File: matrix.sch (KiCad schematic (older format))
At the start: 173 parts

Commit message: Add indicator LEDs
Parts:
- KBP1-1: footprint MX_Only:MXOnly-2U -> MX_Only:MXOnly-1U
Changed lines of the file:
@@
 F 0 "KBP1-1" H 12900 936 50  0000 C CNN
 F 1 "Keyboard_Switch" H 12900 1000 50  0001 C CNN
-F 2 "MX_Only:MXOnly-2U" H 12900 1105 50  0001 C CNN
+F 2 "MX_Only:MXOnly-1U" H 12900 1105 50  0001 C CNN
 F 3 "" H 12900 1105 50  0001 C CNN
 	2    12900 1100

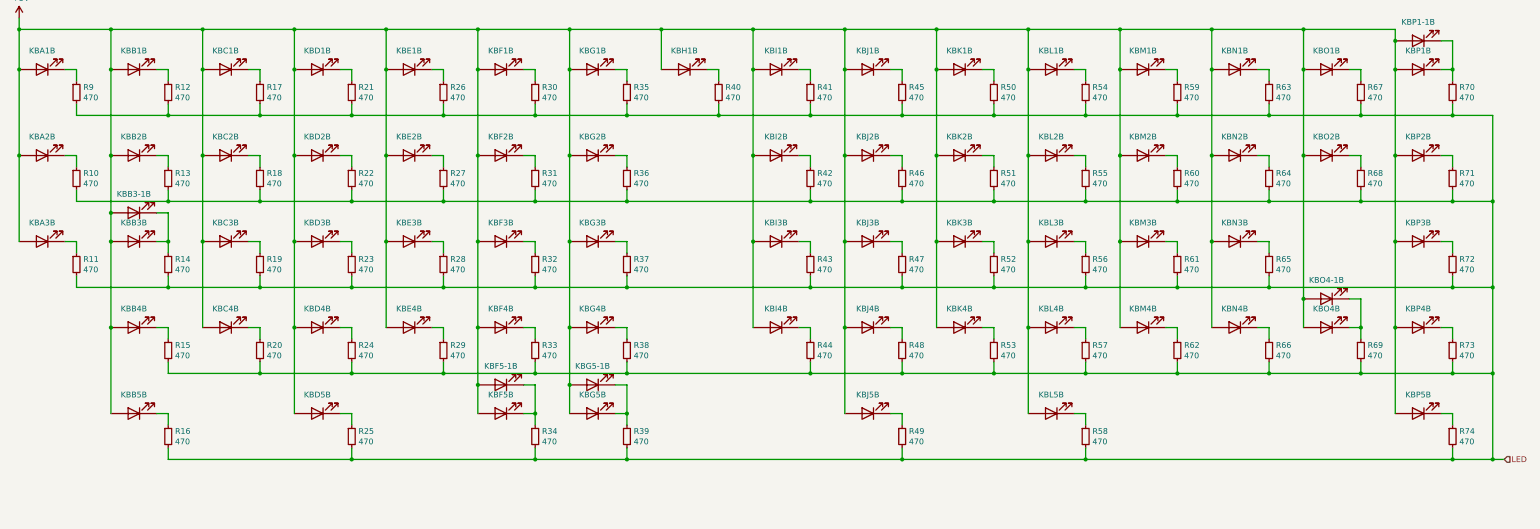
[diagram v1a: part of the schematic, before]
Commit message: Lay out switch and LED matrix components
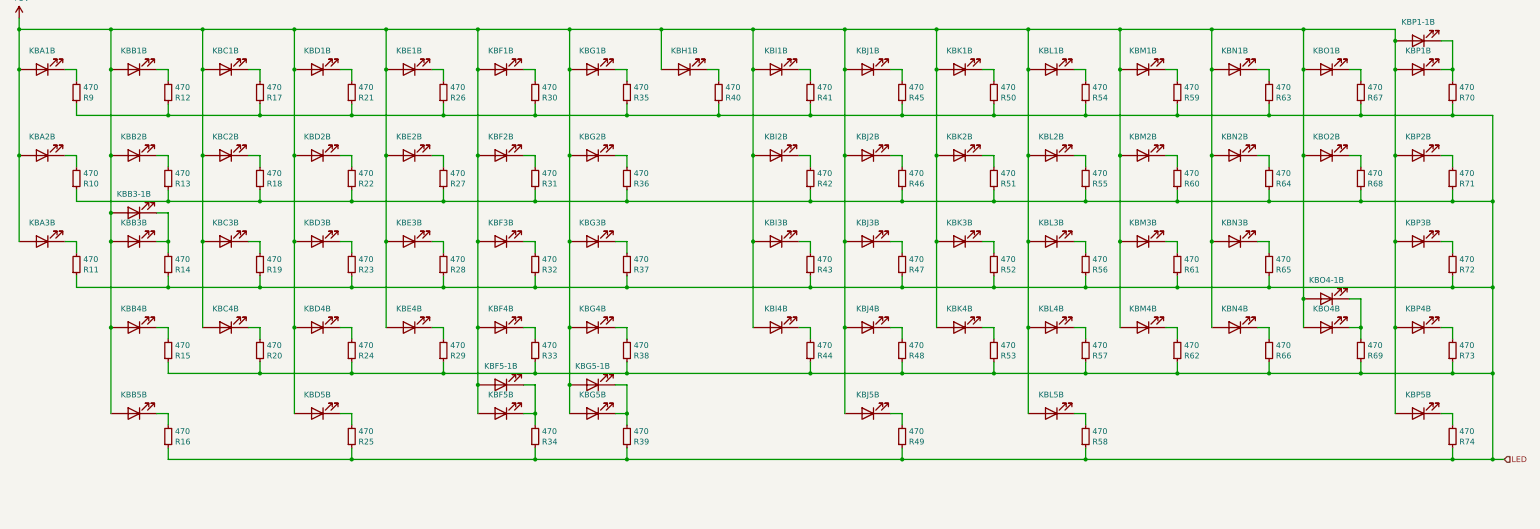
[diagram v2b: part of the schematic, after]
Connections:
- net LED: now also R10.1, R11.1, R12.1, R13.1, R14.1, R15.1, R16.1, R17.1, R18.1, R19.1, R20.1, R21.1, R22.1, R23.1, R24.1, R25.1, R26.1, R27.1, R28.1, R29.1, R30.1, R31.1, R32.1, R33.1, R34.1, R35.1, R36.1, R37.1, R38.1, R39.1, R40.1, R41.1, R42.1, R43.1, R44.1, R45.1, R46.1, R47.1, R48.1, R49.1, R50.1, R51.1, R52.1, R53.1, R54.1, R55.1, R56.1, R57.1, R58.1, R59.1, R60.1, R61.1, R62.1, R63.1, R64.1, R65.1, R66.1, R67.1, R68.1, R69.1, R70.1, R71.1, R72.1, R73.1, R74.1, R9.1; no longer R10.2, R11.2, R12.2, R13.2, R14.2, R15.2, R16.2, R17.2, R18.2, R19.2, R20.2, R21.2, R22.2, R23.2, R24.2, R25.2, R26.2, R27.2, R28.2, R29.2, R30.2, R31.2, R32.2, R33.2, R34.2, R35.2, R36.2, R37.2, R38.2, R39.2, R40.2, R41.2, R42.2, R43.2, R44.2, R45.2, R46.2, R47.2, R48.2, R49.2, R50.2, R51.2, R52.2, R53.2, R54.2, R55.2, R56.2, R57.2, R58.2, R59.2, R60.2, R61.2, R62.2, R63.2, R64.2, R65.2, R66.2, R67.2, R68.2, R69.2, R70.2, R71.2, R72.2, R73.2, R74.2, R9.2
- net at KBF5-1.4 (LEDGND), KBF5.4 (LEDGND): now also R34.2; no longer R34.1
- net at KBG5-1.4 (LEDGND), KBG5.4 (LEDGND): now also R39.2; no longer R39.1
- net at KBP1-1.4 (LEDGND), KBP1.4 (LEDGND): now also R70.2; no longer R70.1
- net at KBO4-1.4 (LEDGND), KBO4.4 (LEDGND): now also R69.2; no longer R69.1
- net at KBA1.4 (LEDGND): now also R9.2; no longer R9.1
- net at KBA2.4 (LEDGND): now also R10.2; no longer R10.1
- net at KBA3.4 (LEDGND): now also R11.2; no longer R11.1
- net at KBB1.4 (LEDGND): now also R12.2; no longer R12.1
- net at KBB2.4 (LEDGND): now also R13.2; no longer R13.1
- net at KBB3-1.4 (LEDGND), KBB3.4 (LEDGND): now also R14.2; no longer R14.1
- net at KBB4.4 (LEDGND): now also R15.2; no longer R15.1
- net at KBB5.4 (LEDGND): now also R16.2; no longer R16.1
- net at KBC1.4 (LEDGND): now also R17.2; no longer R17.1
- net at KBC2.4 (LEDGND): now also R18.2; no longer R18.1
- net at KBC3.4 (LEDGND): now also R19.2; no longer R19.1
- net at KBC4.4 (LEDGND): now also R20.2; no longer R20.1
- net at KBD1.4 (LEDGND): now also R21.2; no longer R21.1
- net at KBD2.4 (LEDGND): now also R22.2; no longer R22.1
- net at KBD3.4 (LEDGND): now also R23.2; no longer R23.1
- net at KBD4.4 (LEDGND): now also R24.2; no longer R24.1
- net at KBD5.4 (LEDGND): now also R25.2; no longer R25.1
- net at KBE1.4 (LEDGND): now also R26.2; no longer R26.1
- net at KBE2.4 (LEDGND): now also R27.2; no longer R27.1
- net at KBE3.4 (LEDGND): now also R28.2; no longer R28.1
- net at KBE4.4 (LEDGND): now also R29.2; no longer R29.1
- net at KBF1.4 (LEDGND): now also R30.2; no longer R30.1
- net at KBF2.4 (LEDGND): now also R31.2; no longer R31.1
- net at KBF3.4 (LEDGND): now also R32.2; no longer R32.1
- net at KBF4.4 (LEDGND): now also R33.2; no longer R33.1
- net at KBG1.4 (LEDGND): now also R35.2; no longer R35.1
- net at KBG2.4 (LEDGND): now also R36.2; no longer R36.1
- net at KBG3.4 (LEDGND): now also R37.2; no longer R37.1
- net at KBG4.4 (LEDGND): now also R38.2; no longer R38.1
- net at KBH1.4 (LEDGND): now also R40.2; no longer R40.1
- net at KBI1.4 (LEDGND): now also R41.2; no longer R41.1
- net at KBI2.4 (LEDGND): now also R42.2; no longer R42.1
- net at KBI3.4 (LEDGND): now also R43.2; no longer R43.1
- net at KBI4.4 (LEDGND): now also R44.2; no longer R44.1
- net at KBJ1.4 (LEDGND): now also R45.2; no longer R45.1
- net at KBJ2.4 (LEDGND): now also R46.2; no longer R46.1
- net at KBJ3.4 (LEDGND): now also R47.2; no longer R47.1
- net at KBJ4.4 (LEDGND): now also R48.2; no longer R48.1
- net at KBJ5.4 (LEDGND): now also R49.2; no longer R49.1
- net at KBK1.4 (LEDGND): now also R50.2; no longer R50.1
- net at KBK2.4 (LEDGND): now also R51.2; no longer R51.1
- net at KBK3.4 (LEDGND): now also R52.2; no longer R52.1
- net at KBK4.4 (LEDGND): now also R53.2; no longer R53.1
- net at KBL1.4 (LEDGND): now also R54.2; no longer R54.1
- net at KBL2.4 (LEDGND): now also R55.2; no longer R55.1
- net at KBL3.4 (LEDGND): now also R56.2; no longer R56.1
- net at KBL4.4 (LEDGND): now also R57.2; no longer R57.1
- net at KBL5.4 (LEDGND): now also R58.2; no longer R58.1
- net at KBM1.4 (LEDGND): now also R59.2; no longer R59.1
- net at KBM2.4 (LEDGND): now also R60.2; no longer R60.1
- net at KBM3.4 (LEDGND): now also R61.2; no longer R61.1
- net at KBM4.4 (LEDGND): now also R62.2; no longer R62.1
- net at KBN1.4 (LEDGND): now also R63.2; no longer R63.1
- net at KBN2.4 (LEDGND): now also R64.2; no longer R64.1
- net at KBN3.4 (LEDGND): now also R65.2; no longer R65.1
- net at KBN4.4 (LEDGND): now also R66.2; no longer R66.1
- net at KBO1.4 (LEDGND): now also R67.2; no longer R67.1
- net at KBO2.4 (LEDGND): now also R68.2; no longer R68.1
- net at KBP2.4 (LEDGND): now also R71.2; no longer R71.1
- net at KBP3.4 (LEDGND): now also R72.2; no longer R72.1
- net at KBP4.4 (LEDGND): now also R73.2; no longer R73.1
- net at KBP5.4 (LEDGND): now also R74.2; no longer R74.1

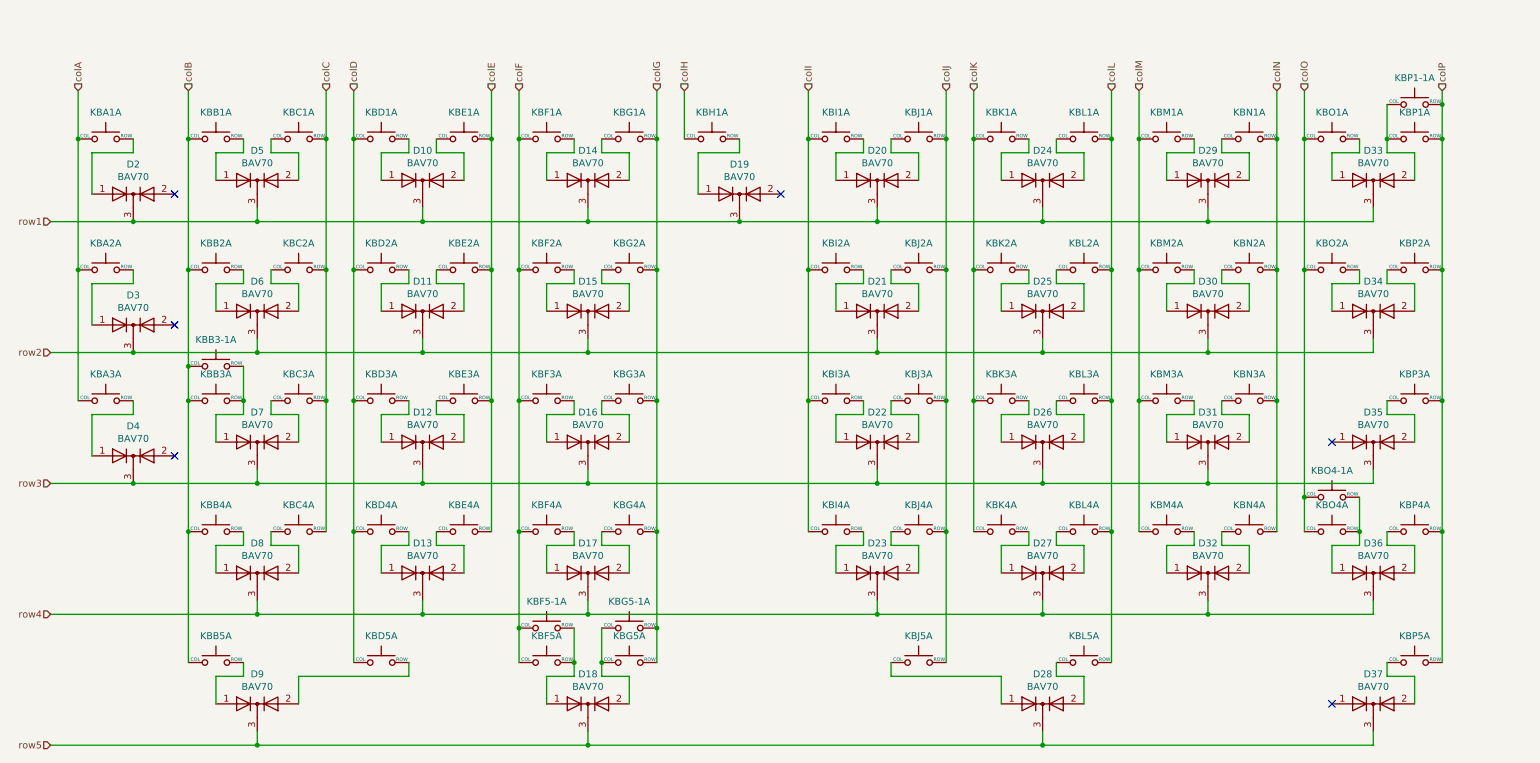
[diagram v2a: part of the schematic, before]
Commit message: Finish routing LED matrix
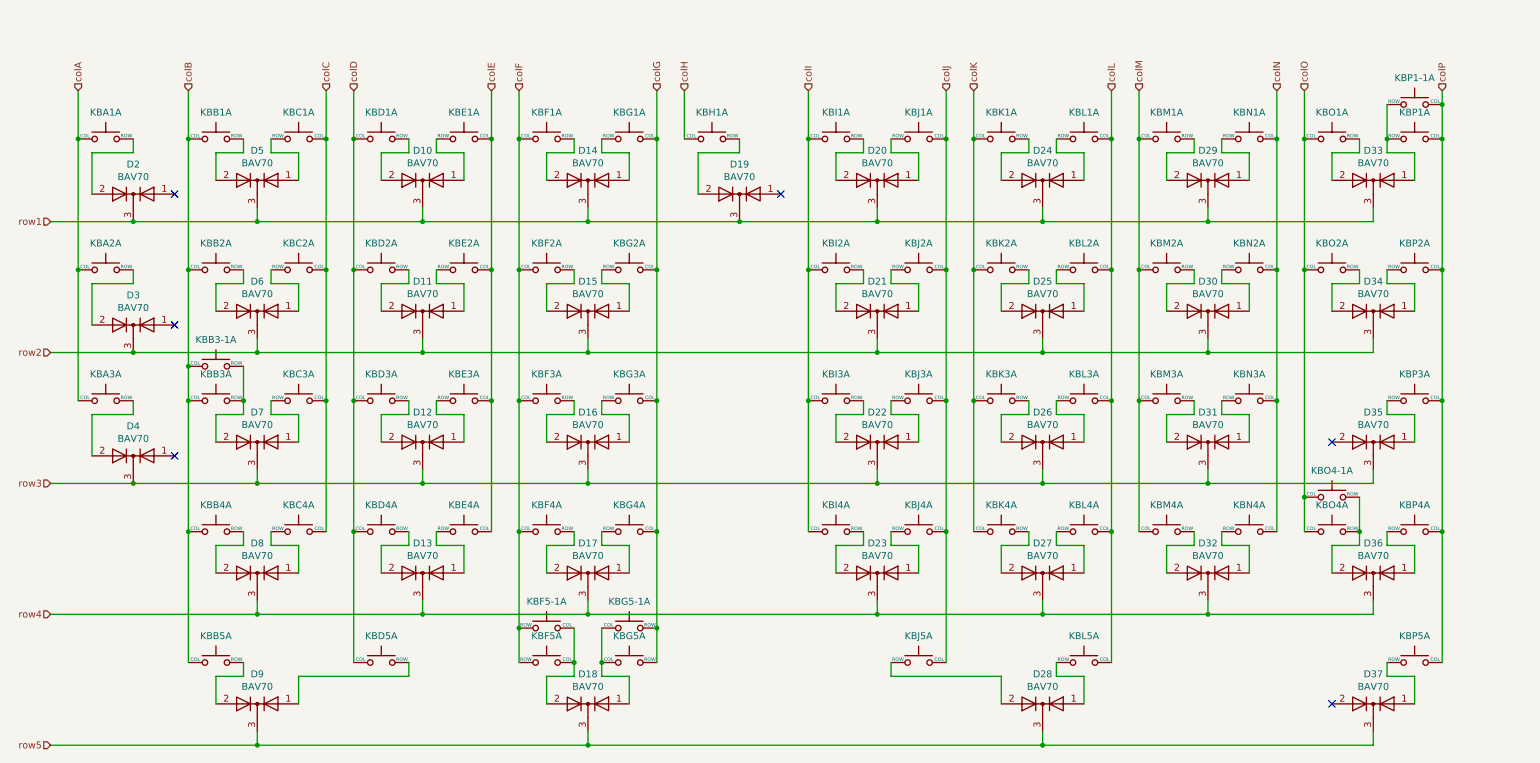
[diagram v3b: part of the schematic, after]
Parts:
- KBP1-1: footprint MX_Only:MXOnly-1U -> MX_Only:MXOnly-1U-FLIPPED
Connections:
- net colC: now also KBC1.1 (COL), KBC2.1 (COL), KBC3.1 (COL), KBC4.1 (COL); no longer KBC1.2 (ROW), KBC2.2 (ROW), KBC3.2 (ROW), KBC4.2 (ROW)
- net colE: now also KBE1.1 (COL), KBE2.1 (COL), KBE3.1 (COL), KBE4.1 (COL); no longer KBE1.2 (ROW), KBE2.2 (ROW), KBE3.2 (ROW), KBE4.2 (ROW)
- net colF: now also KBF5-1.2 (ROW), KBF5.2 (ROW); no longer KBF5-1.1 (COL), KBF5.1 (COL)
- net colG: now also KBG1.1 (COL), KBG2.1 (COL), KBG3.1 (COL), KBG4.1 (COL); no longer KBG1.2 (ROW), KBG2.2 (ROW), KBG3.2 (ROW), KBG4.2 (ROW)
- net colJ: now also KBJ1.1 (COL), KBJ2.1 (COL), KBJ3.1 (COL), KBJ4.1 (COL), KBJ5.1 (COL); no longer KBJ1.2 (ROW), KBJ2.2 (ROW), KBJ3.2 (ROW), KBJ4.2 (ROW), KBJ5.2 (ROW)
- net colL: now also KBL1.1 (COL), KBL2.1 (COL), KBL3.1 (COL), KBL4.1 (COL), KBL5.1 (COL); no longer KBL1.2 (ROW), KBL2.2 (ROW), KBL3.2 (ROW), KBL4.2 (ROW), KBL5.2 (ROW)
- net colN: now also KBN1.1 (COL), KBN2.1 (COL), KBN3.1 (COL), KBN4.1 (COL); no longer KBN1.2 (ROW), KBN2.2 (ROW), KBN3.2 (ROW), KBN4.2 (ROW)
- net colP: now also KBP1-1.1 (COL), KBP1.1 (COL), KBP2.1 (COL), KBP3.1 (COL), KBP4.1 (COL), KBP5.1 (COL); no longer KBP1-1.2 (ROW), KBP1.2 (ROW), KBP2.2 (ROW), KBP3.2 (ROW), KBP4.2 (ROW), KBP5.2 (ROW)
- net at KBA1.2 (ROW): now also D2.2 (A); no longer D2.1 (A)
- net at KBB1.2 (ROW): now also D5.2 (A); no longer D5.1 (A)
- net at KBD1.2 (ROW): now also D10.2 (A); no longer D10.1 (A)
- net at KBF1.2 (ROW): now also D14.2 (A); no longer D14.1 (A)
- net at KBH1.2 (ROW): now also D19.2 (A); no longer D19.1 (A)
- net at KBI1.2 (ROW): now also D20.2 (A); no longer D20.1 (A)
- net at KBK1.2 (ROW): now also D24.2 (A); no longer D24.1 (A)
- net at KBM1.2 (ROW): now also D29.2 (A); no longer D29.1 (A)
- net at KBO1.2 (ROW): now also D33.2 (A); no longer D33.1 (A)
- net at KBA2.2 (ROW): now also D3.2 (A); no longer D3.1 (A)
- net at KBB2.2 (ROW): now also D6.2 (A); no longer D6.1 (A)
- net at KBD2.2 (ROW): now also D11.2 (A); no longer D11.1 (A)
- net at KBF2.2 (ROW): now also D15.2 (A); no longer D15.1 (A)
- net at KBI2.2 (ROW): now also D21.2 (A); no longer D21.1 (A)
- net at KBK2.2 (ROW): now also D25.2 (A); no longer D25.1 (A)
- net at KBM2.2 (ROW): now also D30.2 (A); no longer D30.1 (A)
- net at KBO2.2 (ROW): now also D34.2 (A); no longer D34.1 (A)
- net at KBA3.2 (ROW): now also D4.2 (A); no longer D4.1 (A)
- net at KBB3-1.2 (ROW), KBB3.2 (ROW): now also D7.2 (A); no longer D7.1 (A)
- net at KBD3.2 (ROW): now also D12.2 (A); no longer D12.1 (A)
- net at KBF3.2 (ROW): now also D16.2 (A); no longer D16.1 (A)
- net at KBI3.2 (ROW): now also D22.2 (A); no longer D22.1 (A)
- net at KBK3.2 (ROW): now also D26.2 (A); no longer D26.1 (A)
- net at KBM3.2 (ROW): now also D31.2 (A); no longer D31.1 (A)
- net at D35.2 (A): no longer KBP3.1 (COL)
- net at KBB4.2 (ROW): now also D8.2 (A); no longer D8.1 (A)
- net at KBD4.2 (ROW): now also D13.2 (A); no longer D13.1 (A)
- net at KBF4.2 (ROW): now also D17.2 (A); no longer D17.1 (A)
- net at KBI4.2 (ROW): now also D23.2 (A); no longer D23.1 (A)
- net at KBK4.2 (ROW): now also D27.2 (A); no longer D27.1 (A)
- net at KBM4.2 (ROW): now also D32.2 (A); no longer D32.1 (A)
- net at KBO4-1.2 (ROW), KBO4.2 (ROW): now also D36.2 (A); no longer D36.1 (A)
- net at KBB5.2 (ROW): now also D9.2 (A); no longer D9.1 (A)
- net at KBD5.2 (ROW): now also D9.1 (A); no longer D9.2 (A)
- net at KBG5-1.1 (COL), KBG5.1 (COL): now also D18.1 (A); no longer D18.2 (A)
- net at D28.1 (A): now also KBL5.2 (ROW); no longer KBJ5.1 (COL)
- net at D28.2 (A): now also KBJ5.2 (ROW); no longer KBL5.1 (COL)
- net at D37.2 (A): no longer KBP5.1 (COL)
- net at D35.1 (A): now also KBP3.2 (ROW)
- net at D37.1 (A): now also KBP5.2 (ROW)
- new net: D5.1 (A), KBC1.2 (ROW)
- new net: D10.1 (A), KBE1.2 (ROW)
- new net: D14.1 (A), KBG1.2 (ROW)
- new net: D20.1 (A), KBJ1.2 (ROW)
- new net: D24.1 (A), KBL1.2 (ROW)
- new net: D29.1 (A), KBN1.2 (ROW)
- new net: D33.1 (A), KBP1-1.2 (ROW), KBP1.2 (ROW)
- new net: D6.1 (A), KBC2.2 (ROW)
- new net: D11.1 (A), KBE2.2 (ROW)
- new net: D15.1 (A), KBG2.2 (ROW)
- new net: D21.1 (A), KBJ2.2 (ROW)
- new net: D25.1 (A), KBL2.2 (ROW)
- new net: D30.1 (A), KBN2.2 (ROW)
- new net: D34.1 (A), KBP2.2 (ROW)
- new net: D7.1 (A), KBC3.2 (ROW)
- new net: D12.1 (A), KBE3.2 (ROW)
- new net: D16.1 (A), KBG3.2 (ROW)
- new net: D22.1 (A), KBJ3.2 (ROW)
- new net: D26.1 (A), KBL3.2 (ROW)
- new net: D31.1 (A), KBN3.2 (ROW)
- new net: D8.1 (A), KBC4.2 (ROW)
- new net: D13.1 (A), KBE4.2 (ROW)
- new net: D17.1 (A), KBG4.2 (ROW)
- new net: D23.1 (A), KBJ4.2 (ROW)
- new net: D27.1 (A), KBL4.2 (ROW)
- new net: D32.1 (A), KBN4.2 (ROW)
- new net: D36.1 (A), KBP4.2 (ROW)
- new net: D18.2 (A), KBF5-1.1 (COL), KBF5.1 (COL)
